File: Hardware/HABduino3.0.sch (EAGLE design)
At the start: 40 parts, among them IC2 TPS61201, U1 ARDUINO_SHIELDNO_SILK, U2 LM3480IM3-3.3, U3 TXS0102DCTT

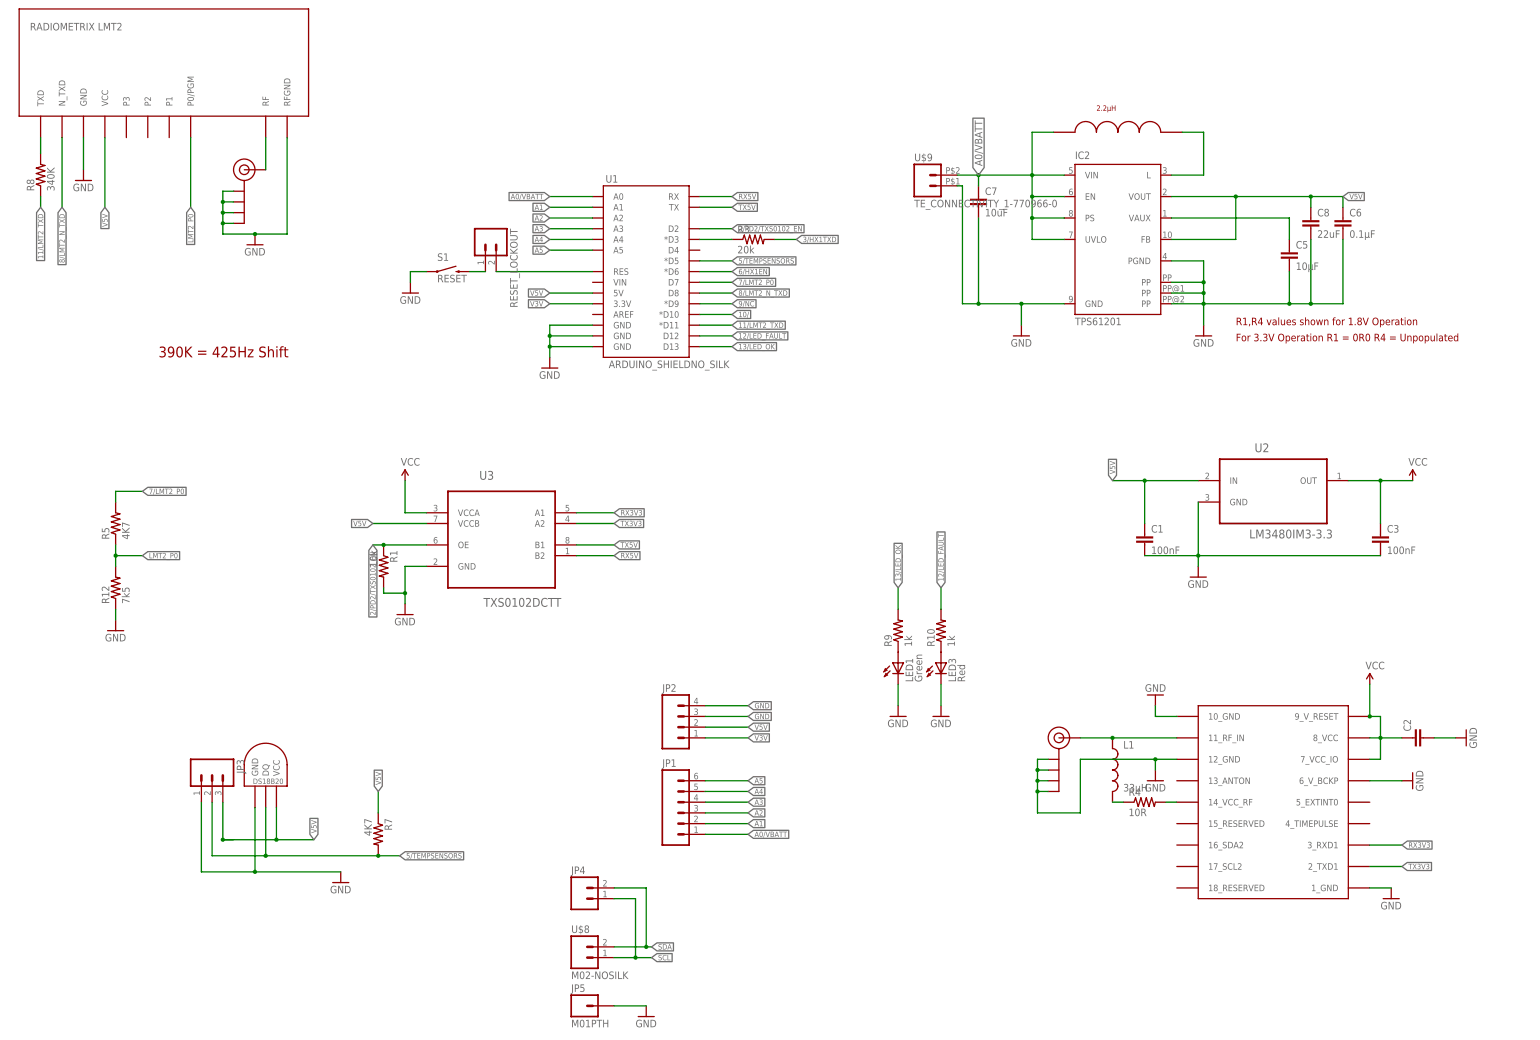
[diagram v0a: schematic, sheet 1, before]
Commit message: New hardware version 3.0
Removed LMT2 and replaced with MTX2 transmitter.
Removed TO92 DS18B20 and replaced with SMD version.
Removed Reset Protect + Reset switch
Switch power supply +/- round to match the Pi In The Sky.
Minor Silk Screen amendments.
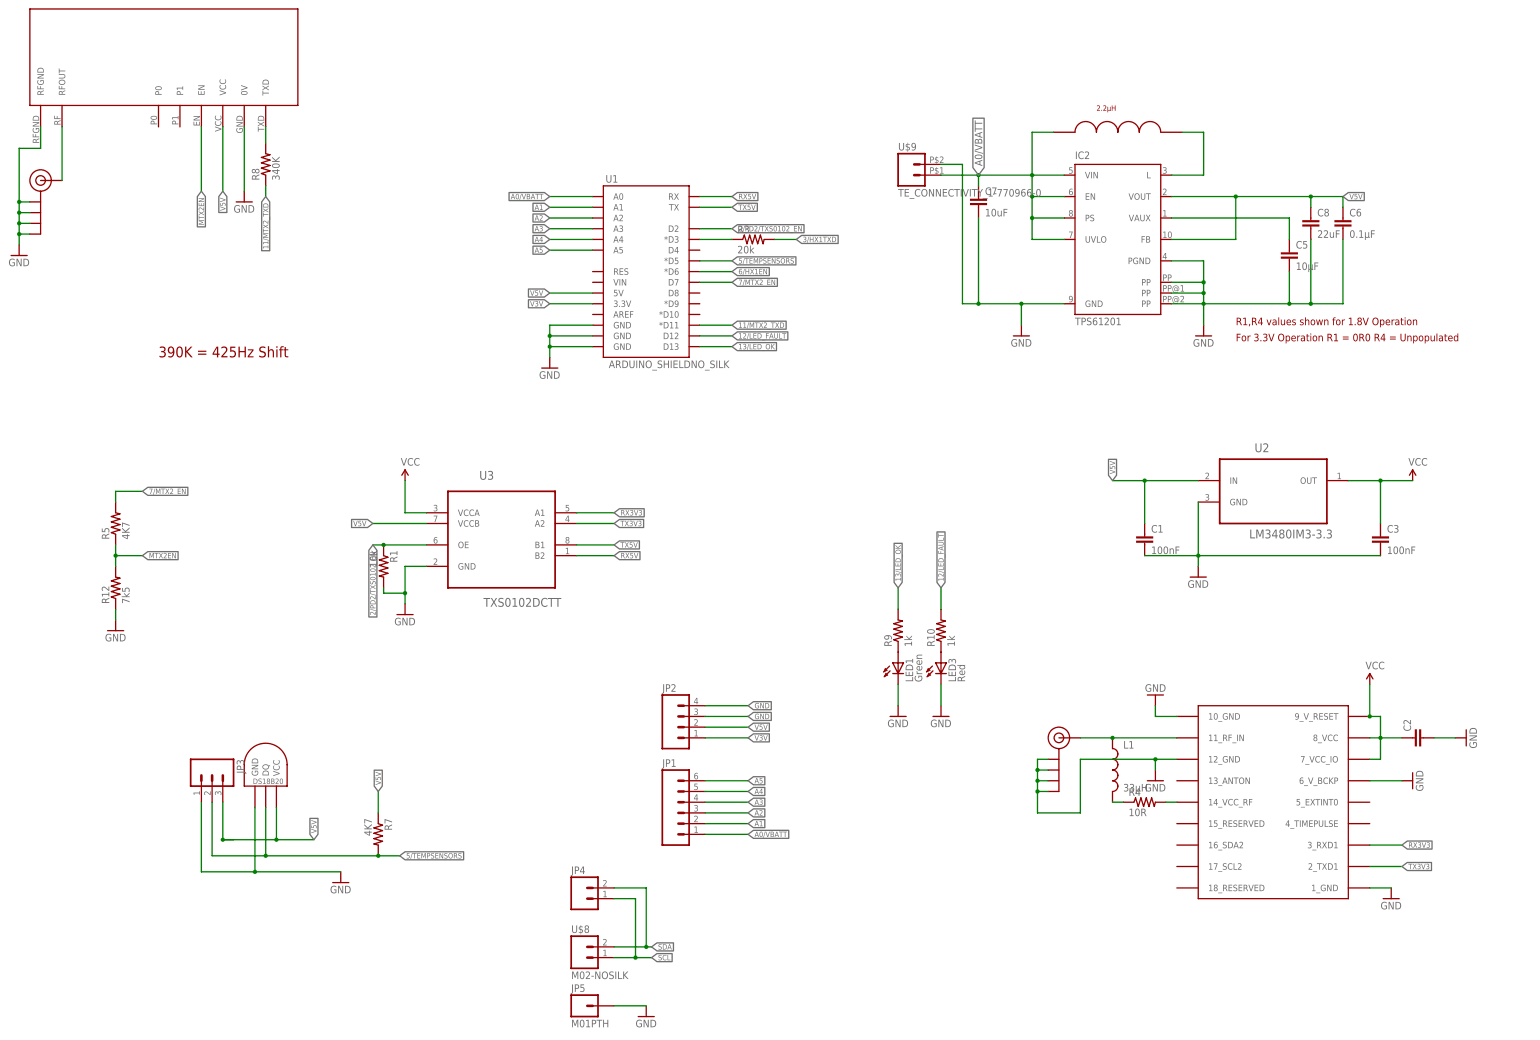
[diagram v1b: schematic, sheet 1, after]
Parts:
- removed RESET_LOCKOUT: (no value), SparkFun:M02PTH
- removed S1: RESET, SparkFun:SWITCH-MOMENTARY-2
- removed TEMPINT: DS1821, ava:DS1820TO92
- removed U$2: RADIOMETRIX_LMT2, ava:RADIOMETRIX_LMT2
- added TEMP: DS1821, ava:DS1820SOIC
- added U$4: RADIOMETRIX-MTX2, ava:RADIOMETRIX-MTX2
- U$1: value UBLOX_MAX-6 -> UBLOX_MAX; device ava:UBLOX_MAX-6 -> ava:UBLOX_MAX
- renumbered U$10 to LPS4018
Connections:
- net 11/LMT2_TXD renamed 11/MTX2_TXD
- net 7/LMT2_P0 renamed 7/MTX2_EN
- removed net 10/: U1.*D10
- removed net 8/LMT2_N_TXD: U$2.N_TXD, U1.D8
- removed net 9/NC: U1.*D9
- removed net LMT2_P0: R12.2, R5.1, U$2.P0/PGM
- removed net N$6: RESET_LOCKOUT.1, S1.2
- removed net _LMT2TXD: R8.2, U$2.TXD
- new net MTX2EN: R12.2, R5.1, U$4.EN
- net 5/TEMPSENSORS: now also TEMP.DQ; no longer TEMPINT.DQ
- net A0/VBATT: now also U$9.1; no longer U$9.2
- net GND: now also TEMP.GND, U$4.0V, U$4.RFGND, U$9.2; no longer S1.1, TEMPINT.GND, U$2.GND, U$2.RFGND, U$9.1
- net N$3: now also U$4.RFOUT; no longer U$2.RF
- net N$7: now also R8.2, U$4.TXD; no longer RESET_LOCKOUT.2, U1.RES
- net V5V: now also TEMP.VCC, U$4.VCC; no longer TEMPINT.VCC, U$2.VCC
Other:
- moved on the sheet: R8, U$9
